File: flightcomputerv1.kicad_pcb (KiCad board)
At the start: 2 copper layers, 127.2 x 76.2 mm, 51 parts, among them IC1 MMC5983MA, J1 Screw_Terminal_01x02, J2 Screw_Terminal_01x02, J5 Conn_01x02, J6 Conn_01x24, J7 Conn_01x24, J8 Conn_Coaxial, J9 Conn_Coaxial, M1 Motor_Servo, M2 Motor_Servo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

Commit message: updated pcb + backups
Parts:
- moved J2 9.40 mm to (137.0, 61.5)
- moved J1 8.70 mm to (128.0, 55.0)
- moved R4 7.81 mm to (119.1, 61.5)
- moved R3 4.06 mm to (119.1, 63.5)
- moved R2 1.70 mm to (119.1, 67.5)
- moved R1 1.45 mm to (119.1, 65.5)
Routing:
- net /VBATT: track 0.00 -> 35.5 mm
- net /ldo_5v: track 0.00 -> 34.3 mm
- net GND: track 0.00 -> 30.8 mm
- net /buzz_pwm: track 0.00 -> 22.1 mm
- net Net-(J2-Pin_2): track 0.00 -> 9.64 mm
- net Net-(J1-Pin_1): track 0.00 -> 8.33 mm
- net Net-(Q1-G2): track 0.00 -> 8.17 mm
- net Net-(Q1-G1): track 0.00 -> 5.51 mm
- net Net-(Q3-B): track 0.00 -> 2.53 mm
- net Net-(Q2-B): track 0.00 -> 2.23 mm

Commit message: updated pcb
routing more but they're kinda sus
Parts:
- moved SW1 19.4 mm to (140.8, 89.8)
- moved U6 19.3 mm to (126.0, 97.0)
- moved J9 15.0 mm to (159.5, 97.5)
- moved J8 9.64 mm to (151.5, 84.8)
- moved C10 8.27 mm to (137.0, 110.5)
- moved J2 6.57 mm to (138.0, 55.0)
- moved R8 1.79 mm to (152.5, 71.9), turned to -90 degrees
- moved SW2 0.75 mm to (122.7, 78.7)
- moved R7 0.74 mm to (150.7, 71.9), turned to -90 degrees
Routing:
- net /teensy_3.3v: track 0.00 -> 135.9 mm
- net /GPS_int: track 0.00 -> 83.9 mm
- net /GPS_reset: track 0.00 -> 80.3 mm
- net /radio_dio3: track 0.00 -> 76.5 mm
- net /radio_dio5: track 0.00 -> 74.1 mm
- net /radio_dio4: track 0.00 -> 67.9 mm
- net /radio_dio0: track 0.00 -> 53.2 mm
- net /radio_dio2: track 0.00 -> 53.1 mm
- net Net-(U1-PROGRAM): track 0.00 -> 38.9 mm
- net Net-(J9-In): track 0.00 -> 29.8 mm
- net /teensy_onoff: track 0.00 -> 20.9 mm
- net /PYRO1: track 0.00 -> 18.0 mm
- net Net-(J8-In): track 0.00 -> 16.5 mm
- net /GPS_sda: track 0.00 -> 9.88 mm
- net /GPS_scl: track 0.00 -> 9.62 mm
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
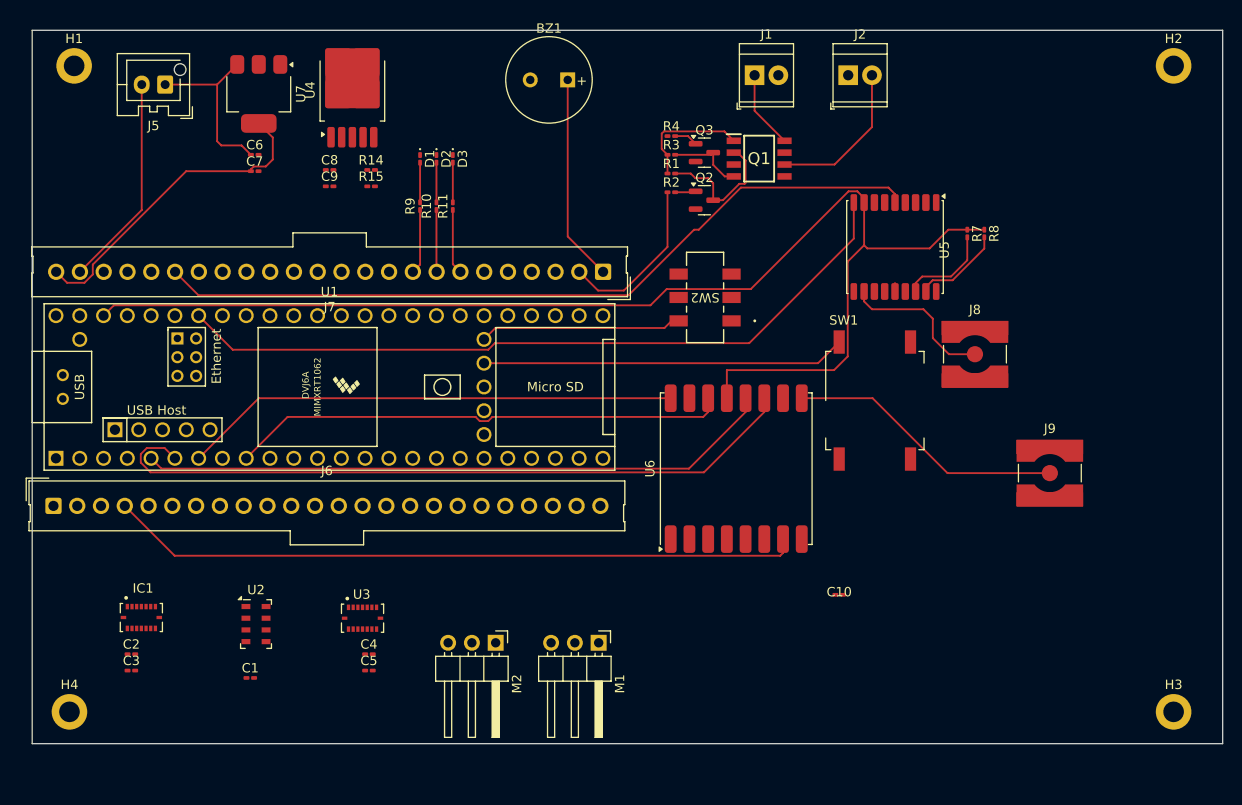
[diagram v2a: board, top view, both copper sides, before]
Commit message: signal traces can via through the board
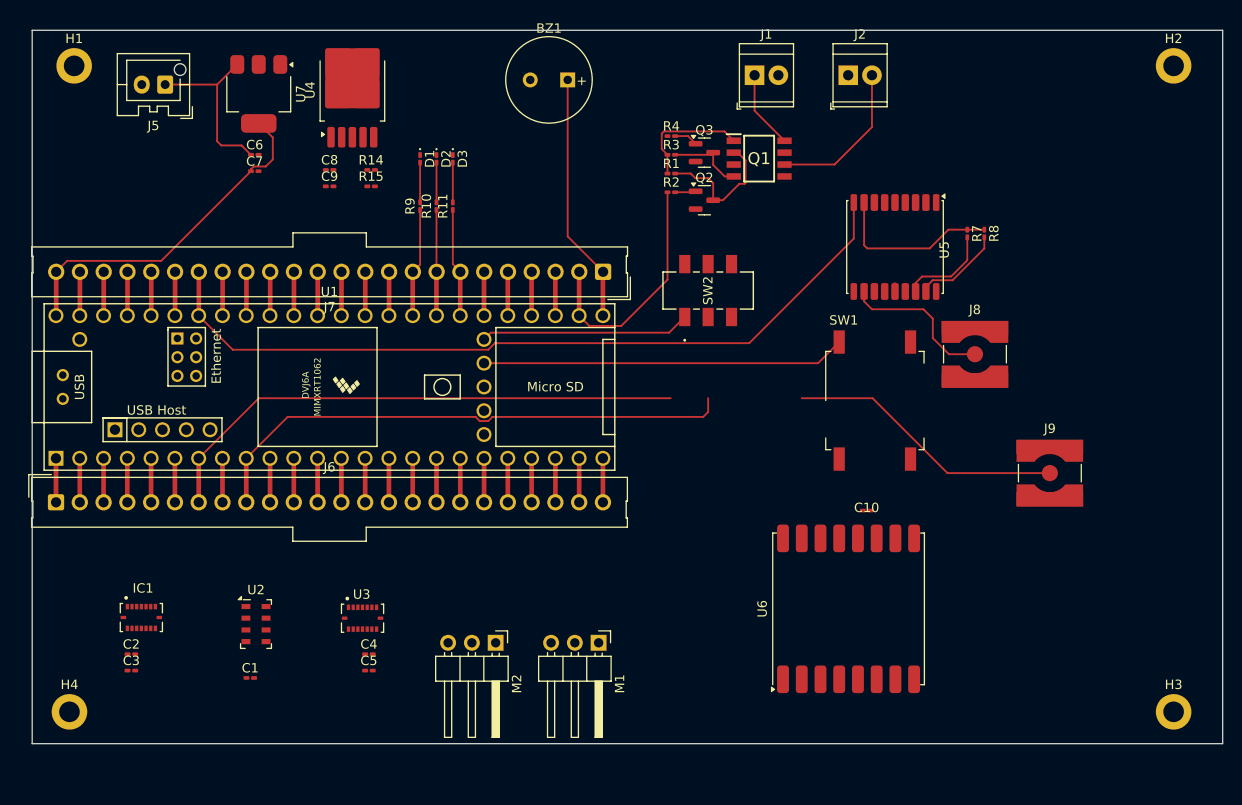
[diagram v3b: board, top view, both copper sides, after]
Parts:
- moved U6 19.2 mm to (138.0, 112.0)
- moved C10 9.47 mm to (139.9, 101.5)
- moved SW2 0.81 mm to (123.0, 78.0), turned to 90 degrees
- moved J6 0.47 mm to (53.3, 100.6)
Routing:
- net /teensy_3.3v: track 135.9 -> 28.7 mm
- net /GPS_int: track 83.9 -> 4.69 mm
- net /radio_dio3: track 76.5 -> 4.70 mm
- net /radio_dio5: track 74.1 -> 4.70 mm
- net /radio_dio4: track 67.9 -> 4.70 mm
- net GND: track 22.7 -> 14.1 mm
- net /PYRO1: track 18.0 -> 26.2 mm
- net /servo2_pwm: track 0.00 -> 4.70 mm
- net /SENSE_mosi: track 0.00 -> 4.70 mm
- net /FREE2: track 0.00 -> 4.70 mm
- net /radio_dio2: track 53.1 -> 57.8 mm
- net /radio_dio0: track 53.2 -> 57.9 mm
- net /servo1_pwm: track 0.00 -> 4.70 mm
- net /radio_sck: track 0.00 -> 4.70 mm
- net /radio_reset: track 0.00 -> 4.70 mm
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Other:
- copper layers 2 -> 4

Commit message: updated placement and routing 2/16
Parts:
- removed SW1: SW_MEC_5G, Button_Switch_SMD:SW_MEC_5GSH9
- added S1: TS04-66-70-BK-160-SMT, HPRfootprints:SW_TS04-66-70-BK-160-SMT, F.Cu at (131.2, 88.0)
- SW2: value SLW-913535-2A-SMT -> SW_Wuerth_450301014042; footprint HPRfootprints:SLW-913535_CUD -> Button_Switch_THT:SW_Slide-03_Wuerth-WS-SLTV_10x2.5x6.4_P2.54mm
- moved U4 65.3 mm to (56.8, 115.5), turned to 180 degrees
- moved C8 55.6 mm to (65.3, 117.9), turned to 90 degrees
- moved C9 53.4 mm to (67.0, 117.9), turned to 90 degrees
- moved R14 53.0 mm to (65.3, 113.5), turned to 90 degrees
- moved R15 50.7 mm to (67.0, 113.5), turned to 90 degrees
- moved J1 30.2 mm to (97.7, 55.0)
- moved J2 24.0 mm to (114.0, 55.1)
- moved Q1 23.0 mm to (107.0, 55.5), turned to 90 degrees
- moved U7 20.2 mm to (56.0, 64.0), turned to 0 degrees
- moved BZ1 20.0 mm to (128.0, 56.5), turned to 0 degrees
- moved Q3 16.4 mm to (106.4, 61.3), turned to 90 degrees
- moved R4 14.9 mm to (104.6, 64.9), turned to 90 degrees
- moved R7 14.5 mm to (136.2, 70.4)
- moved R8 14.5 mm to (138.0, 70.4)
- moved U5 14.5 mm to (128.5, 71.8)
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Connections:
- J6 pad 11: /FREE2 -> /mag_int
- J6 pad 16: /FREE3 -> /imu_accel_int1
- J6 pad 17: /FREE4 -> /imu_gyro_int1
- SW2 pad 3: GND -> /teensy_3.3v
- U1 pad 11: /FREE2 -> /mag_int
- U1 pad 16: /FREE3 -> /imu_accel_int1
- U1 pad 17: /FREE4 -> /imu_gyro_int1
- U6 pad 15: /radio_dio2 -> /radio_dio1
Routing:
- net /radio_dio0: track 57.9 -> 4.70 mm
- net /radio_dio2: track 57.8 -> 4.70 mm
- net Net-(U1-PROGRAM): track 38.9 -> 0.00 mm
- net Net-(J9-In): track 29.8 -> 0.00 mm
- net /SENSE_miso: track 4.70 -> 30.6 mm
- net /ldo_5v: track 37.4 -> 12.1 mm
- net /teensy_onoff: track 22.4 -> 0.00 mm
- net /buzz_pwm: track 26.8 -> 4.69 mm
- net /SENSE_mosi: track 4.70 -> 26.1 mm
- net /PYRO1: track 26.2 -> 4.93 mm
- net /GPS_reset: track 84.9 -> 64.4 mm
- net /imu_gyro_int1: track 0.00 -> 19.1 mm
- net /servo1_pwm: track 4.70 -> 22.7 mm
- net Net-(J2-Pin_2): track 16.5 -> 0.00 mm
- net Net-(J8-In): track 16.5 -> 0.00 mm
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- added copper zone on In2.Cu, net /teensy_3.3v
- added copper zone on In1.Cu, net GND

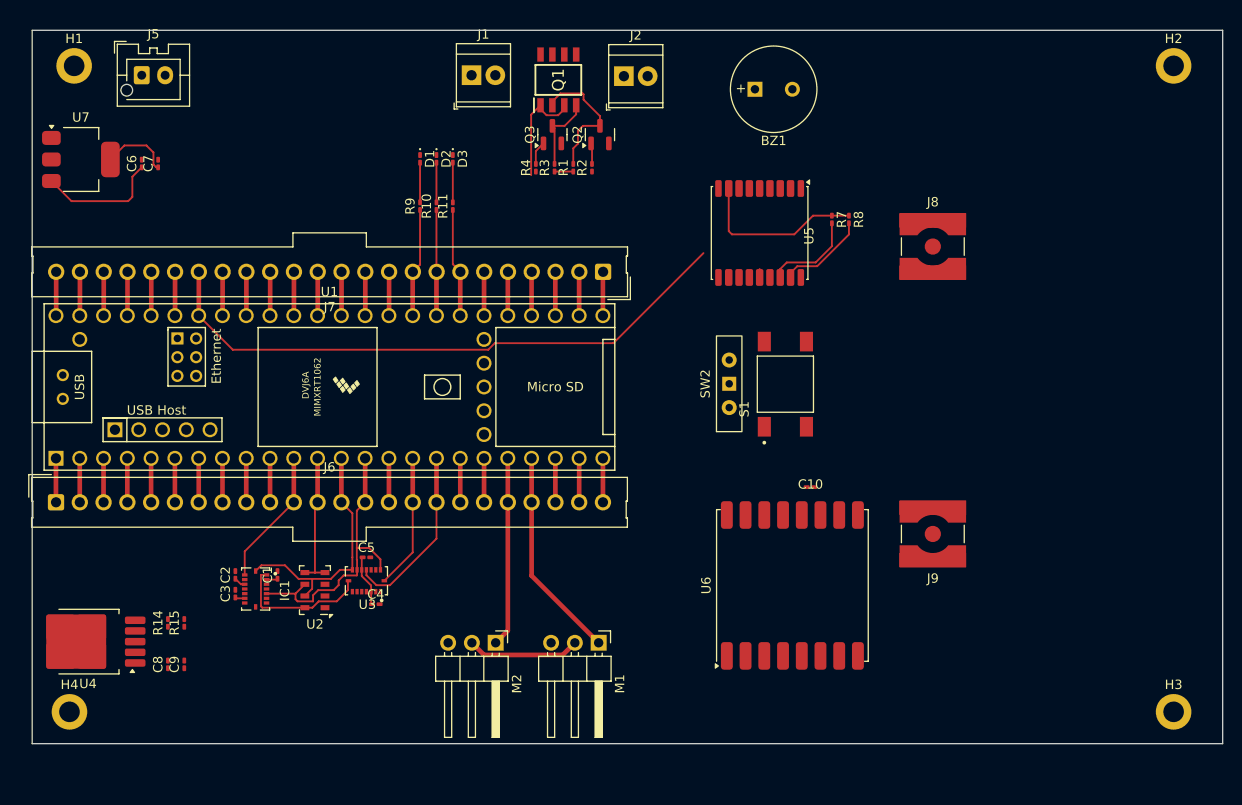
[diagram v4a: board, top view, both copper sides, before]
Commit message: finished most of routing 2/28
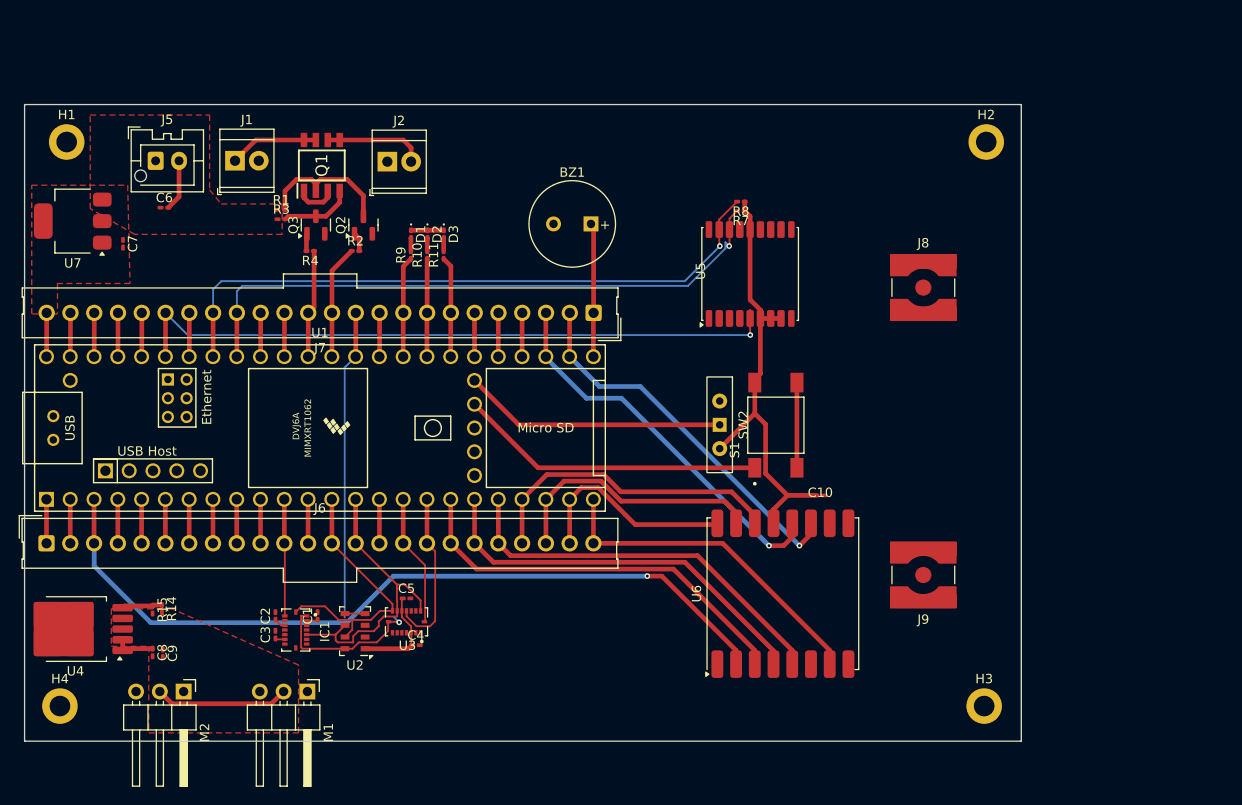
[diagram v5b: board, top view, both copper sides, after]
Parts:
- moved M2 33.7 mm to (67.0, 120.8)
- moved M1 31.5 mm to (80.2, 120.8)
- moved R1 31.5 mm to (77.4, 69.4), turned to 0 degrees
- moved R3 29.7 mm to (77.4, 70.4), turned to 0 degrees
- moved Q2 27.0 mm to (86.2, 71.0)
- moved Q3 27.0 mm to (81.1, 71.0)
- moved J1 26.9 mm to (72.5, 64.1)
- moved Q1 26.9 mm to (81.7, 64.6)
- moved J2 26.9 mm to (88.7, 64.2)
- moved R2 26.8 mm to (85.3, 73.8), turned to 0 degrees
- moved R4 25.7 mm to (80.5, 73.8), turned to 180 degrees
- moved BZ1 22.7 mm to (110.5, 70.9), turned to 180 degrees
- moved H2 21.6 mm to (152.7, 62.1)
- moved H3 20.2 mm to (152.5, 122.4)
- moved R8 11.7 mm to (126.5, 68.5), turned to 180 degrees
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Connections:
- J6 pad 20: /servo2_pwm -> /radio_cs
- J6 pad 21: /servo1_pwm -> /radio_dio0
- J6 pad 22: /FREE5 -> /radio_dio1
- J6 pad 23: /FREE6 -> /radio_dio2
- J6 pad 24: /radio_cs -> /radio_dio5
- J6 pad 4: /radio_dio5 -> /FREE11
- J6 pad 5: /radio_dio4 -> /FREE12
- J6 pad 6: /radio_dio3 -> /FREE6
- J6 pad 7: /radio_dio2 -> /servo2_pwm
- J6 pad 8: /radio_dio1 -> /servo1_pwm
- J6 pad 9: /radio_dio0 -> /FREE5
- J7 pad 12: /FREE12 -> /PYRO1
- J7 pad 13: /FREE11 -> /PYRO2
- J7 pad 2: /PYRO1 -> /radio_dio3
- J7 pad 3: /PYRO2 -> /radio_dio4
- U1 pad 20: /servo2_pwm -> /radio_cs
- U1 pad 21: /servo1_pwm -> /radio_dio0
- U1 pad 22: /FREE5 -> /radio_dio1
- U1 pad 23: /FREE6 -> /radio_dio2
- U1 pad 24: /radio_cs -> /radio_dio5
- U1 pad 26: /PYRO1 -> /radio_dio3
- U1 pad 27: /PYRO2 -> /radio_dio4
- U1 pad 36: /FREE12 -> /PYRO1
- U1 pad 37: /FREE11 -> /PYRO2
- U1 pad 4: /radio_dio5 -> /FREE11
- U1 pad 5: /radio_dio4 -> /FREE12
- U1 pad 6: /radio_dio3 -> /FREE6
- U1 pad 7: /radio_dio2 -> /servo2_pwm
- U1 pad 8: /radio_dio1 -> /servo1_pwm
- U1 pad 9: /radio_dio0 -> /FREE5
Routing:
- net /radio_miso: track 4.70 -> 85.2 mm, vias 0 -> 1
- net /GPS_int: track 4.69 -> 71.5 mm, vias 0 -> 1
- net /GPS_reset: track 64.4 -> 4.69 mm
- net /GPS_scl: track 14.3 -> 68.8 mm, vias 0 -> 1
- net /GPS_sda: track 14.6 -> 66.4 mm, vias 0 -> 1
- net /radio_mosi: track 4.70 -> 43.4 mm
- net /radio_sck: track 4.70 -> 42.8 mm
- net /radio_cs: track 4.70 -> 42.3 mm
- net /radio_dio4: track 4.70 -> 41.4 mm, vias 0 -> 1
- net /radio_dio3: track 4.70 -> 40.8 mm, vias 0 -> 1
- net /teensy_3.3v: track 36.6 -> 71.0 mm
- net Net-(U1-PROGRAM): track 0.00 -> 32.8 mm
- net /radio_dio5: track 4.70 -> 36.1 mm
- net /SENSE_sck: track 19.8 -> 50.0 mm, vias 0 -> 1
- net /radio_dio0: track 4.70 -> 33.3 mm
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- added copper zone on F.Cu, net /VBATT
- added copper zone on F.Cu, net /ldo_5v
- added copper zone on F.Cu, net /ldo_6v
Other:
- board size 127.2 x 76.2 mm -> 106.5 x 68 mm

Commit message: prelim routing placement done 3/2 need to check batt connector footprints + antenna connector + backup radio
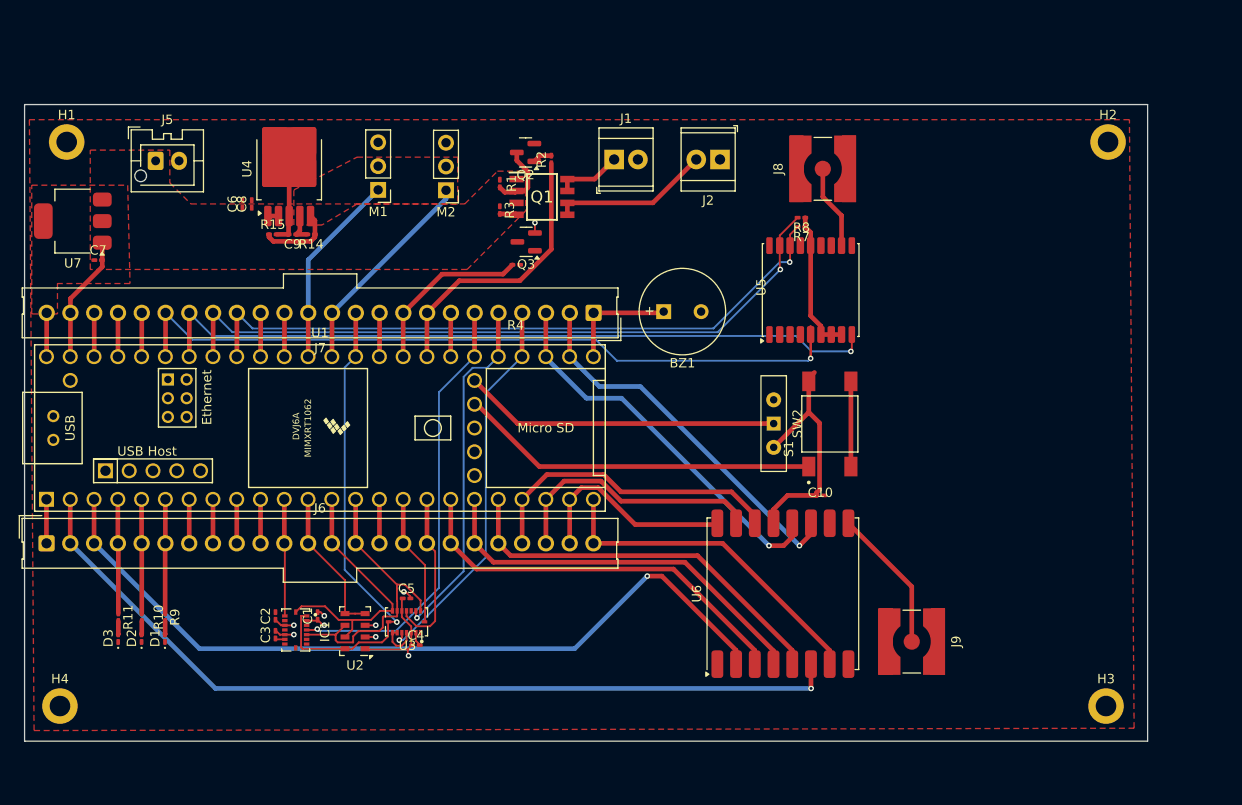
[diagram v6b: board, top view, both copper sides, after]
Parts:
- M1, M2: footprint Connector_PinHeader_2.54mm:PinHeader_1x03_P2.54mm_Horizontal -> Connector_PinHeader_2.54mm:PinHeader_1x03_P2.54mm_Vertical
- moved M2 60.4 mm to (95.0, 67.3), turned to 180 degrees
- moved D3 55.4 mm to (60.0, 115.1), turned to 90 degrees
- moved U4 54.2 mm to (78.2, 65.0), turned to 90 degrees
- moved M1 54.1 mm to (87.8, 67.2), turned to 180 degrees
- moved D2 52.9 mm to (62.5, 115.1), turned to 90 degrees
- moved R11 52.0 mm to (60.0, 112.9), turned to -90 degrees
- moved D1 50.5 mm to (65.0, 115.1), turned to 90 degrees
- moved R10 49.3 mm to (62.5, 112.9), turned to -90 degrees
- moved C8 49.1 mm to (74.2, 68.8), turned to 90 degrees
- moved C9 46.8 mm to (78.6, 72.0), turned to 180 degrees
- moved R9 46.7 mm to (65.0, 112.9), turned to -90 degrees
- moved R14 43.1 mm to (80.6, 72.0), turned to 180 degrees
- moved R15 42.1 mm to (76.5, 72.0), turned to 0 degrees
- moved J1 40.5 mm to (113.0, 64.0)
- moved J2 35.5 mm to (124.3, 64.0), turned to 180 degrees
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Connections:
- J6 pad 4: /FREE11 -> /LED3
- J6 pad 5: /FREE12 -> /LED2
- J6 pad 6: /FREE6 -> /LED1
- J6 pad 7: /servo2_pwm -> /FREE11
- J6 pad 8: /servo1_pwm -> /FREE12
- J7 pad 12: /PYRO1 -> /servo2_pwm
- J7 pad 13: /PYRO2 -> /servo1_pwm
- J7 pad 7: /LED3 -> /FREE6
- J7 pad 8: /LED2 -> /PYRO1
- J7 pad 9: /LED1 -> /PYRO2
- U1 pad 31: /LED3 -> /FREE6
- U1 pad 32: /LED2 -> /PYRO1
- U1 pad 33: /LED1 -> /PYRO2
- U1 pad 36: /PYRO1 -> /servo2_pwm
- U1 pad 37: /PYRO2 -> /servo1_pwm
- U1 pad 4: /FREE11 -> /LED3
- U1 pad 5: /FREE12 -> /LED2
- U1 pad 6: /FREE6 -> /LED1
- U1 pad 7: /servo2_pwm -> /FREE11
- U1 pad 8: /servo1_pwm -> /FREE12
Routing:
- net /radio_reset: track 4.70 -> 92.8 mm, vias 0 -> 1
- net /GPS_reset: track 4.69 -> 78.9 mm, vias 0 -> 1
- net /mag_cs: track 4.69 -> 47.1 mm, vias 0 -> 1
- net /imu_gyro_cs: track 4.69 -> 41.5 mm, vias 0 -> 1
- net /imu_accel_cs: track 4.69 -> 37.9 mm, vias 0 -> 1
- net GND: track 32.2 -> 55.6 mm, vias 0 -> 6
- net /servo2_pwm: track 4.70 -> 22.8 mm
- net /PYRO1: track 12.2 -> 30.0 mm
- net /servo1_pwm: track 4.70 -> 20.9 mm
- net Net-(J9-In): track 0.00 -> 15.4 mm
- net /GPS_int: track 71.5 -> 82.6 mm
- net /ldo_6v: track 14.3 -> 3.31 mm
- net /baro_cs: track 7.25 -> 16.4 mm
- net Net-(J8-In): track 0.00 -> 9.03 mm
- net /VBATT: track 9.27 -> 1.41 mm
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- added copper zone on F.Cu, net GND
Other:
- board size 106.5 x 68 mm -> 120 x 68 mm
